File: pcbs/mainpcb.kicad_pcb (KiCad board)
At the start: 2 copper layers, 219.4 x 133.6 mm, 99 parts, among them J1 TRRS, J2 TRRS, J3 12pin FPC, J4 Female 9pin, J5 Female 9pin, J6 Male 9pin, J7 Male 9pin, SW1 TRRS, SW10 TRRS, SW11 TRRS, SW12 TRRS, SW13 TRRS, SW14 TRRS, SW15 TRRS, SW16 TRRS, SW17 TRRS, SW18 TRRS, SW19 TRRS, SW2 TRRS, SW20 TRRS, SW21 TRRS, SW22 TRRS, SW23 TRRS, SW24 TRRS, SW25 TRRS, SW26 TRRS, SW27 TRRS, SW28 TRRS, SW29 TRRS, SW3 TRRS, SW30 TRRS, SW31 TRRS, SW32 TRRS, SW33 TRRS, SW34 TRRS, SW35 TRRS, SW36 TRRS, SW4 TRRS, SW5 TRRS, SW6 TRRS, SW7 TRRS, SW8 TRRS, SW9 TRRS, U1 Pro Micro Footprint, U2 Pro Micro Footprint

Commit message: I can't believe I learned freecad for this + mounting holes
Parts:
- added H1: M2, kbd:M2_HOLE_v3, F.Cu at (27.0, -15.0)
- added H10: M2, kbd:M2_HOLE_v3, F.Cu at (-67.0, -4.50)
- added H11: M2, kbd:M2_HOLE_v3, F.Cu at (36.0, 8.50)
- added H12: M2, kbd:M2_HOLE_v3, F.Cu at (-31.0, 8.50)
- added H13: M2, kbd:M2_HOLE_v3, F.Cu at (35.5, 52.1)
- added H14: M2, kbd:M2_HOLE_v3, F.Cu at (71.5, 31.3)
- added H15: M2, kbd:M2_HOLE_v3, F.Cu at (71.5, 72.9)
- added H2: M2, kbd:M2_HOLE_v3, F.Cu at (-22.0, -15.0)
- added H3: M2, kbd:M2_HOLE_v3, F.Cu at (46.0, -43.5)
- added H4: M2, kbd:M2_HOLE_v3, F.Cu at (-41.0, -43.5)
- added H5: M2, kbd:M2_HOLE_v3, F.Cu at (73.0, -41.5)
- added H6: M2, kbd:M2_HOLE_v3, F.Cu at (-68.0, -41.5)
- added H7: M2, kbd:M2_HOLE_v3, F.Cu at (92.0, -24.5)
- added H8: M2, kbd:M2_HOLE_v3, F.Cu at (-87.0, -24.5)
- added H9: M2, kbd:M2_HOLE_v3, F.Cu at (72.0, -4.50)
- D1, D10, D11, D12, D13, D14, D15, D16, D17, D18, D19, D2, D20, D21, D22, D23, D24, D25, D26, D27, D28, D29, D3, D30, D31, D32, D33, D34, D35, D36, D4, D5, D6, D7, D8, D9: footprint kbd:D3_TH_SMD_v2 -> Library:D3_TH_SMD_v2
- J3: moved to F.Cu
- SW1, SW10, SW11, SW12, SW13, SW14, SW15, SW16, SW17, SW18, SW19, SW2, SW20, SW21, SW22, SW23, SW24, SW25, SW26, SW27, SW28, SW29, SW3, SW30, SW31, SW32, SW33, SW34, SW35, SW36, SW4, SW5, SW6, SW7, SW8, SW9: value TRRS -> Val**
- moved J4 4.00 mm to (78.0, 52.1)
- moved J5 4.00 mm to (-73.0, 52.1)
- moved J3 2.00 mm to (59.5, 52.1), turned to -90 degrees
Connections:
- net c1_r1 renamed c1_r4
- net c2_r1 renamed c2_r4
- net mirror_c1_r1 renamed mirror_c1_r4
- net mirror_c1_r2 renamed mirror_c1_r5
- net mirror_c2_r1 renamed mirror_c2_r4
- net mirror_c2_r2 renamed mirror_c2_r5
- DS1 pad 2: rgb_ug1_in -> RGB
- DS8 pad 2: rgb_ug1_in -> RGB
- J1 pad 1: TRRS_A -> GND
- J1 pad 2: TRRS_B -> GND
- J1 pad 3: GND -> SERIAL
- J2 pad 1: TRRS_A -> GND
- J2 pad 2: TRRS_B -> GND
- J2 pad 3: GND -> SERIAL
- J3 pad 1: (no net) -> VCC
- J3 pad 2: (no net) -> GND
- J3 pad 3: (no net) -> SDA
- J3 pad 4: (no net) -> SCL
- U1 pad 10: (no net) -> scroll_r2
- U1 pad 11: (no net) -> scroll_r1
- U1 pad 12: (no net) -> R2
- U1 pad 13: (no net) -> RGB
- U1 pad 14: (no net) -> SERIAL
- U1 pad 17: (no net) -> SDA
- U1 pad 18: (no net) -> SCL
- U1 pad 19: (no net) -> C1
- U1 pad 20: (no net) -> C2
- U1 pad 21: (no net) -> C3
- U1 pad 22: (no net) -> C4
- U1 pad 23: (no net) -> C5
- U1 pad 24: (no net) -> R1
- U1 pad 9: (no net) -> scroll_switch
- U2 pad 10: (no net) -> scroll_r2
- U2 pad 11: (no net) -> scroll_r1
- U2 pad 12: (no net) -> R2
- U2 pad 13: (no net) -> RGB
- U2 pad 14: (no net) -> SERIAL
- U2 pad 17: (no net) -> SDA
- U2 pad 18: (no net) -> SCL
- U2 pad 19: (no net) -> C1
- U2 pad 20: (no net) -> C2
- U2 pad 21: (no net) -> C3
- U2 pad 22: (no net) -> C4
- U2 pad 23: (no net) -> C5
- U2 pad 24: (no net) -> R1
- U2 pad 9: (no net) -> scroll_switch
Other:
- board size 219.4 x 133.6 mm -> 219.4 x 139 mm

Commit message: Hopefully finalized layout + more pretty pics and cad
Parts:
- moved J4 6.00 mm to (72.0, 52.1)
- moved J5 6.00 mm to (-67.0, 52.1)
- moved J7 0.50 mm to (-6.49, 15.8)
- moved J6 0.50 mm to (11.5, 15.8)
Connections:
- D18 pad 1: R3_left -> R3
- D19 pad 1: R2_left -> R2
- D20 pad 1: R1_left -> R1
- D21 pad 1: R3_left -> R3
- D22 pad 1: R2_left -> R2
- D23 pad 1: R1_left -> R1
- D24 pad 1: R3_left -> R3
- D25 pad 1: R2_left -> R2
- D26 pad 1: R1_left -> R1
- D27 pad 1: R3_left -> R3
- D28 pad 1: R2_left -> R2
- D29 pad 1: R1_left -> R1
- D30 pad 1: R3_left -> R3
- D31 pad 1: R2_left -> R2
- D32 pad 1: R1_left -> R1
- D33 pad 1: R4_left -> R4
- D34 pad 1: R5_left -> R5
- D35 pad 1: R4_left -> R4
- D36 pad 1: R5_left -> R5
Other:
- outline, holes or cut-outs redrawn

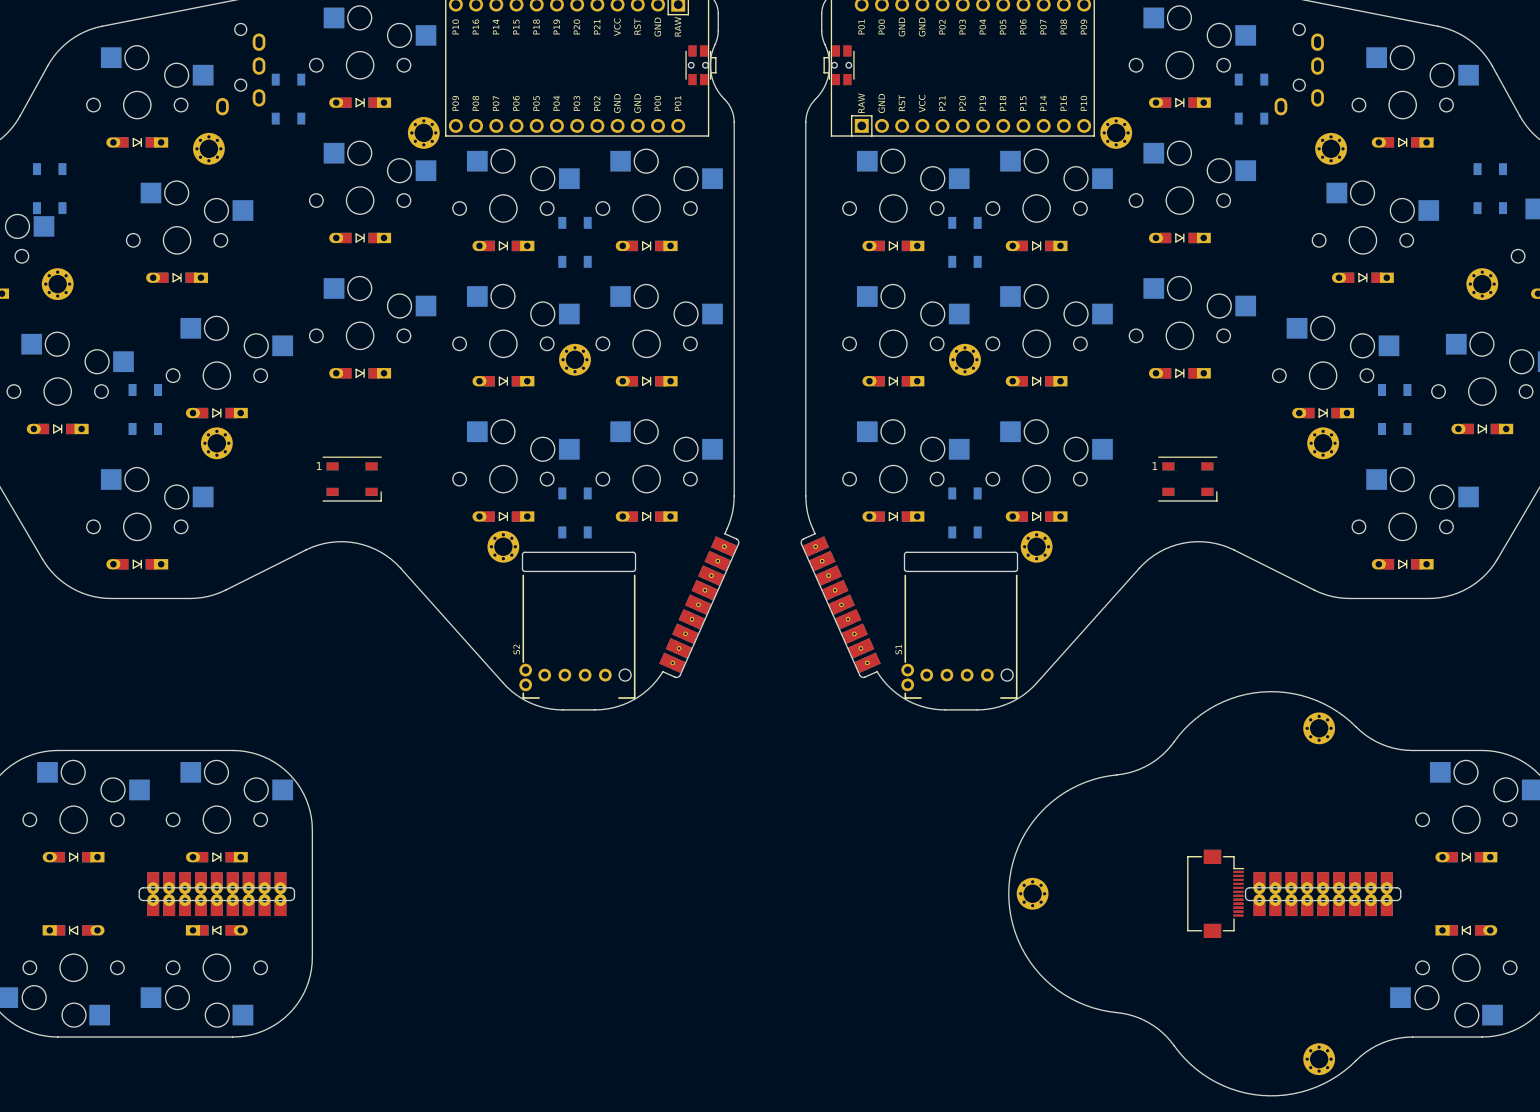
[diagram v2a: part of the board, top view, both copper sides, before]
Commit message: Add resistors
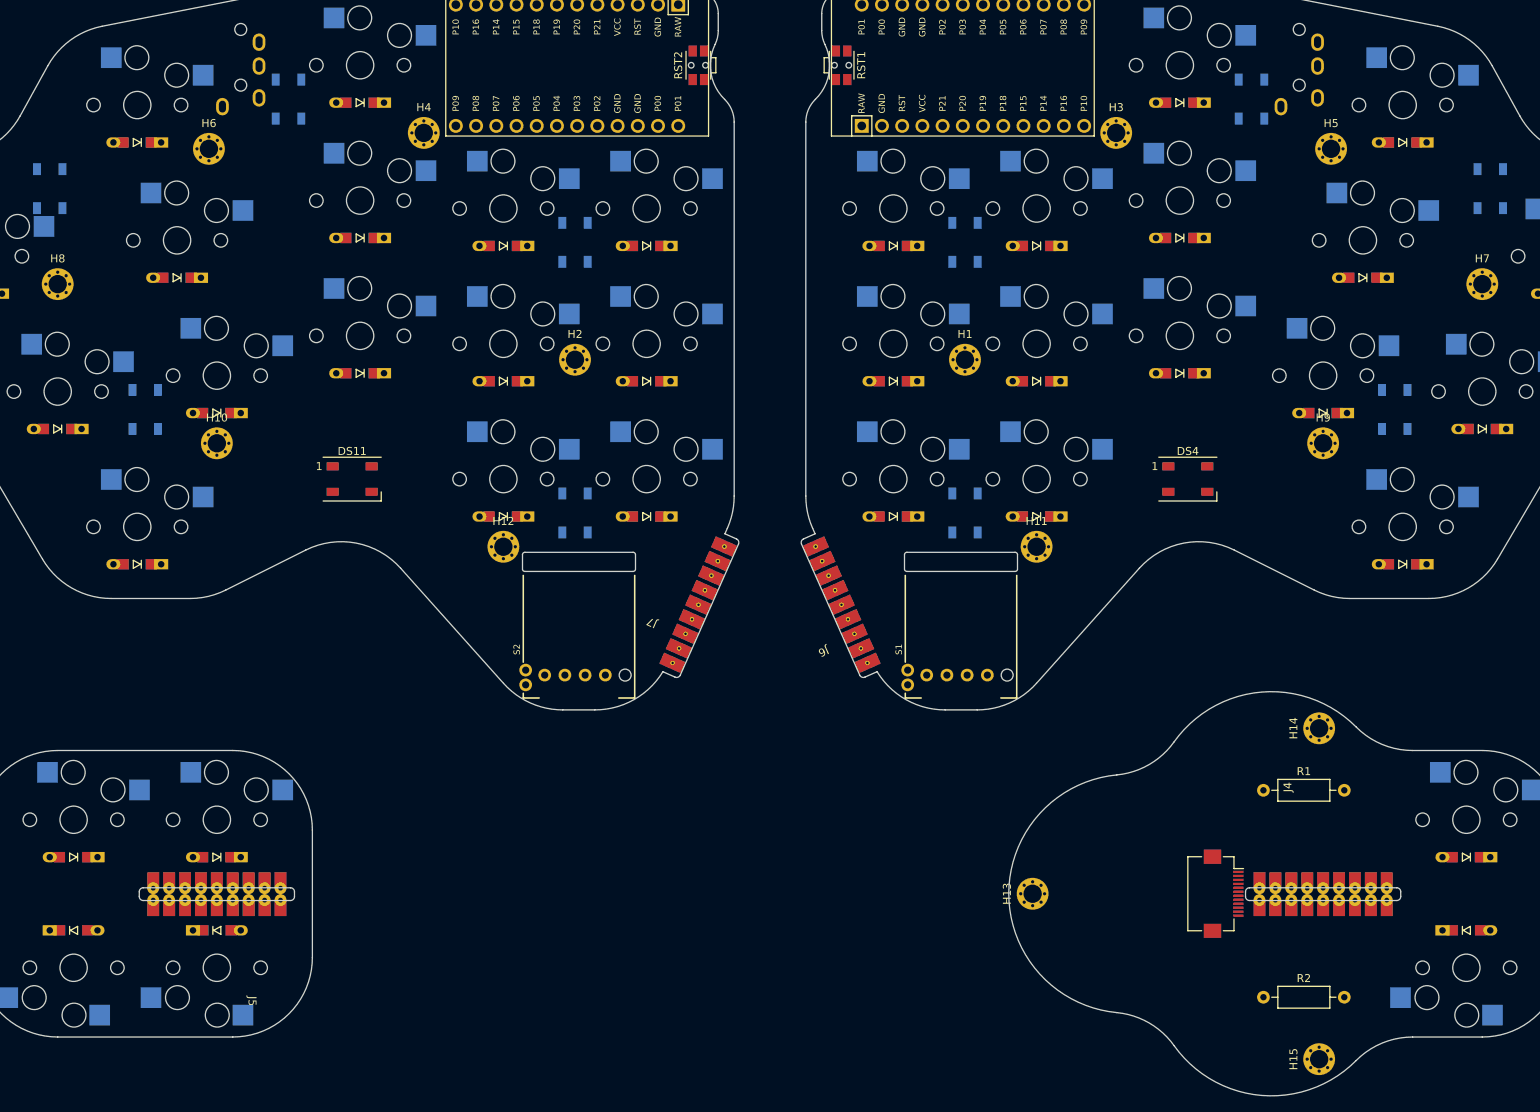
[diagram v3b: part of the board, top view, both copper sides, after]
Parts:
- added R1: 4K7, Resistor_THT:R_Axial_DIN0207_L6.3mm_D2.5mm_P10.16mm_Horizontal, F.Cu at (64.5, 39.1)
- added R2: 4K7, Resistor_THT:R_Axial_DIN0207_L6.3mm_D2.5mm_P10.16mm_Horizontal, F.Cu at (64.5, 65.1)

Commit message: Finish v1 with gerbers?
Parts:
- added J8: Male 9pin, Library:kb_90deg_connector_male_9pin, F.Cu at (11.5, 15.8)
- added J9: Male 9pin, Library:kb_90deg_connector_male_9pin, F.Cu at (-6.49, 15.8)
- J3: value 12pin FPC -> I2C Breakout; footprint Library:Hirose_FH12-12S-0.5SH_1x12-1MP_P0.50mm_Horizontal -> Connector_PinHeader_2.54mm:PinHeader_1x04_P2.54mm_Vertical
- J4: value Female 9pin -> I2C Breakout; footprint Library:kb_90deg_connector_female_9pin -> Connector_PinHeader_2.54mm:PinHeader_1x04_P2.54mm_Vertical
- J5: value Female 9pin -> 12pin FPC; footprint Library:kb_90deg_connector_female_9pin -> Library:Hirose_FH12-12S-0.5SH_1x12-1MP_P0.50mm_Horizontal
- J6, J7: value Male 9pin -> Female 9pin; footprint Library:kb_90deg_connector_male_9pin -> Library:kb_90deg_connector_female_9pin
- moved J4 136.3 mm to (-16.0, -52.0), turned to -90 degrees
- moved J5 126.5 mm to (59.5, 52.1)
- moved J3 111.0 mm to (21.0, -52.0), turned to 90 degrees
- moved J6 70.6 mm to (72.0, 52.1), turned to 90 degrees
- moved J7 70.6 mm to (-67.0, 52.1), turned to -90 degrees
- turned DS14 to 90 degrees
- turned DS3 to 180 degrees
- turned DS4 to 180 degrees
- turned DS5 to -90 degrees
- turned DS6 to -90 degrees
- turned DS8 to 90 degrees
- turned DS9 to 90 degrees
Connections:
- DS1 pad 2: RGB -> rgb_ug1_out
- DS1 pad 4: rgb_ug1_out -> RGB
- DS10 pad 2: rgb_ug2_out -> rgb_ug3_out
- DS10 pad 4: rgb_ug3_out -> rgb_ug2_out
- DS11 pad 2: rgb_ug3_out -> rgb_palm_out
- DS11 pad 4: rgb_palm_out -> rgb_ug3_out
- DS12 pad 2: rgb_palm_out -> rgb_ug4_out
- DS12 pad 4: rgb_ug4_out -> rgb_palm_out
- DS13 pad 2: rgb_ug4_out -> rgb_ug5_out
- DS13 pad 4: rgb_ug5_out -> rgb_ug4_out
- DS14 pad 2: rgb_ug5_out -> rgb_ug6_out
- DS14 pad 4: rgb_ug6_out -> rgb_ug5_out
- DS2 pad 2: rgb_ug1_out -> rgb_ug2_out
- DS2 pad 4: rgb_ug2_out -> rgb_ug1_out
- DS3 pad 2: rgb_ug2_out -> rgb_ug3_out
- DS3 pad 4: rgb_ug3_out -> rgb_ug2_out
- DS4 pad 2: rgb_ug3_out -> rgb_palm_out
- DS4 pad 4: rgb_palm_out -> rgb_ug3_out
- DS5 pad 2: rgb_palm_out -> rgb_ug4_out
- DS5 pad 4: rgb_ug4_out -> rgb_palm_out
- DS6 pad 2: rgb_ug4_out -> rgb_ug5_out
- DS6 pad 4: rgb_ug5_out -> rgb_ug4_out
- DS7 pad 2: rgb_ug5_out -> rgb_ug6_out
- DS7 pad 4: rgb_ug6_out -> rgb_ug5_out
- DS8 pad 2: RGB -> rgb_ug1_out
- DS8 pad 4: rgb_ug1_out -> RGB
- DS9 pad 2: rgb_ug1_out -> rgb_ug2_out
- DS9 pad 4: rgb_ug2_out -> rgb_ug1_out
- J5 pad 5: C1 -> (no net)
- J5 pad 6: C2 -> (no net)
- J5 pad 7: R4 -> (no net)
- J5 pad 8: R5 -> (no net)
- S1 pad S1: scroll_switch -> GND
- S1 pad S2: GND -> scroll_switch
- S2 pad S1: scroll_switch -> GND
- S2 pad S2: GND -> scroll_switch
- U1 pad 10: scroll_r2 -> R4
- U1 pad 11: scroll_r1 -> R3
- U1 pad 6: (no net) -> scroll_switch
- U1 pad 7: (no net) -> scroll_r2
- U1 pad 8: (no net) -> scroll_r1
- U1 pad 9: scroll_switch -> R5
- U2 pad 10: scroll_r2 -> R4
- U2 pad 11: scroll_r1 -> R3
- U2 pad 6: (no net) -> scroll_switch
- U2 pad 7: (no net) -> scroll_r2
- U2 pad 8: (no net) -> scroll_r1
- U2 pad 9: scroll_switch -> R5

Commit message: Add plate generator
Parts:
- SW1, SW10, SW11, SW12, SW13, SW14, SW15, SW16, SW17, SW18, SW19, SW2, SW20, SW21, SW22, SW23, SW24, SW25, SW26, SW27, SW28, SW29, SW3, SW30, SW31, SW32, SW33, SW34, SW35, SW36, SW4, SW5, SW6, SW7, SW8, SW9: value Val** -> PG1350
- turned J8 to -156.038 degrees
- turned J9 to 156.038 degrees
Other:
- board size 219.4 x 139 mm -> 248.2 x 139 mm
- net class Default added: clearance 0.2, trace_width 0.25, via_dia 0.8, via_drill 0.4

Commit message: Add palm led diffuser
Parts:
- added H16: M2, kbd:M2_HOLE_v3, F.Cu at (-57.0, 3.50)
- added H17: M2, kbd:M2_HOLE_v3, F.Cu at (35.5, 52.1)
- added H18: M2, kbd:M2_HOLE_v3, F.Cu at (71.5, 31.3)
- added H19: M2, kbd:M2_HOLE_v3, F.Cu at (71.5, 72.9)
- SW1, SW10, SW11, SW12, SW13, SW14, SW15, SW16, SW17, SW18, SW19, SW2, SW20, SW21, SW22, SW23, SW24, SW25, SW26, SW27, SW28, SW29, SW3, SW30, SW31, SW32, SW33, SW34, SW35, SW36, SW4, SW5, SW6, SW7, SW8, SW9: value PG1350 -> Val**
- moved H14 120.9 mm to (-44.0, -4.50), turned to 0 degrees
- moved H15 70.0 mm to (62.0, 3.50), turned to 0 degrees
- moved H13 58.2 mm to (49.0, -4.50), turned to 0 degrees
- turned J8 to -156.038 degrees
- turned J9 to 156.038 degrees
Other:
- board size 248.2 x 139 mm -> 219.4 x 139 mm
- net class Default removed

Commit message: V2
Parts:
- added J10: SDA, kbd:Jumper, F.Cu at (-28.0, -50.0)
- added J11: 12pin FPC, Library:Hirose_FH12-12S-0.5SH_1x12-1MP_P0.50mm_Horizontal, F.Cu at (59.5, 52.1)
- added J12: Female 9pin, Library:kb_90deg_connector_female_9pin, F.Cu at (72.0, 52.1)
- added J13: Female 9pin, Library:kb_90deg_connector_female_9pin, F.Cu at (-67.0, 52.1)
- added J14: Male 9pin, Library:kb_90deg_connector_male_9pin, F.Cu at (11.3, 16.1)
- added J15: Male 9pin, Library:kb_90deg_connector_male_9pin, F.Cu at (-6.30, 16.1)
- J5: value 12pin FPC -> SDA; footprint Library:Hirose_FH12-12S-0.5SH_1x12-1MP_P0.50mm_Horizontal -> kbd:Jumper
- J6, J7: value Female 9pin -> SDA; footprint Library:kb_90deg_connector_female_9pin -> kbd:Jumper
- J8, J9: value Male 9pin -> SDA; footprint Library:kb_90deg_connector_male_9pin -> kbd:Jumper
- moved J7 142.9 mm to (33.0, -50.0), turned to 0 degrees
- moved J6 111.2 mm to (33.0, -52.0), turned to 0 degrees
- moved J5 109.4 mm to (33.0, -54.0), turned to 0 degrees
- moved J8 80.2 mm to (-28.0, -54.0), turned to 180 degrees
- moved J9 71.1 mm to (-28.0, -52.0), turned to 180 degrees
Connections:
- J1 pad 2: GND -> VCC
- J1 pad 3: SERIAL -> TRRS3
- J1 pad 4: VCC -> TRRS4
- J2 pad 2: GND -> VCC
- J2 pad 3: SERIAL -> TRRS3
- J2 pad 4: VCC -> TRRS4
- J5 pad 1: VCC -> SERIAL
- J5 pad 2: GND -> TRRS3
- J6 pad 1: VCC -> SDA
- J6 pad 2: GND -> TRRS4
- J7 pad 1: VCC -> SCL
- J7 pad 2: GND -> TRRS3
- J8 pad 1: VCC -> SERIAL
- J8 pad 2: GND -> TRRS3
- J9 pad 1: VCC -> SDA
- J9 pad 2: GND -> TRRS4
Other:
- outline, holes or cut-outs redrawn
